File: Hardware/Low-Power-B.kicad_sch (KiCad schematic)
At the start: 25 parts, among them J1 01x02, Q1 BC557, Q2 BC547, Q3 BC557, Q4 BC547, Q5 BC547, U1 Arduino_Pro_Micro, U2 VS1838B

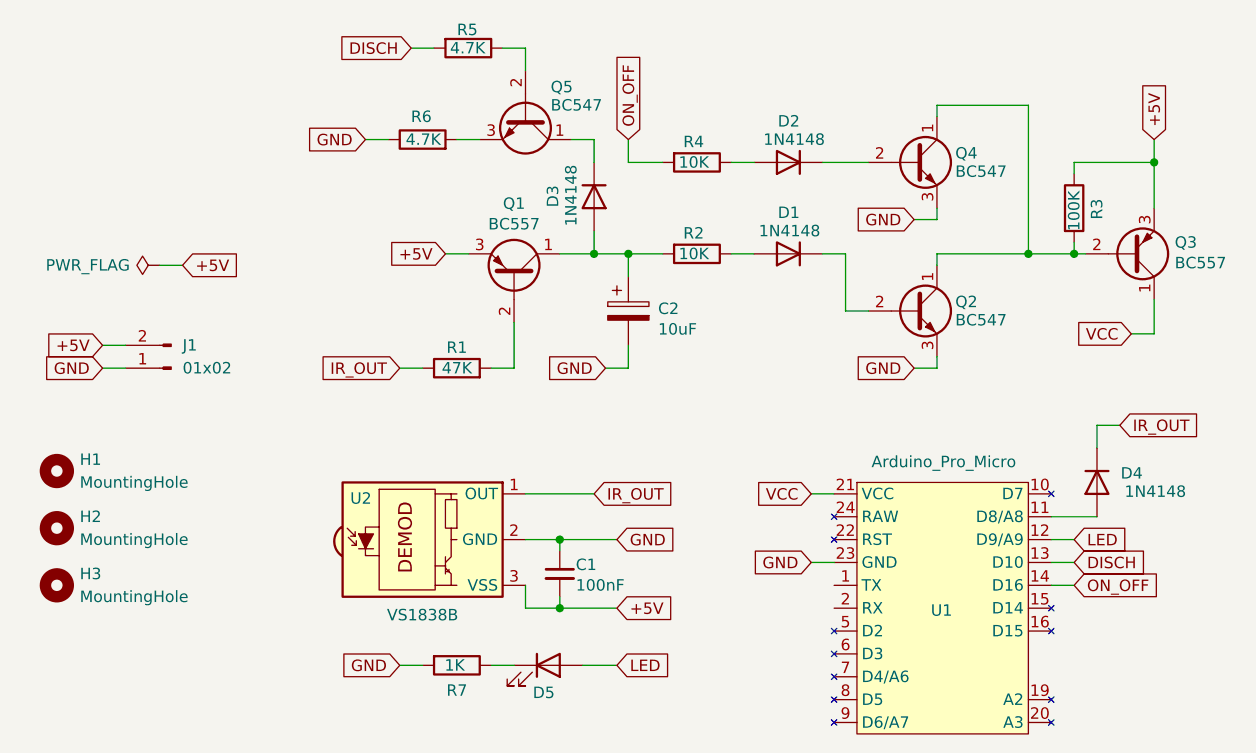
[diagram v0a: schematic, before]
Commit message: Minor fixes on Low-Power-B 3D model
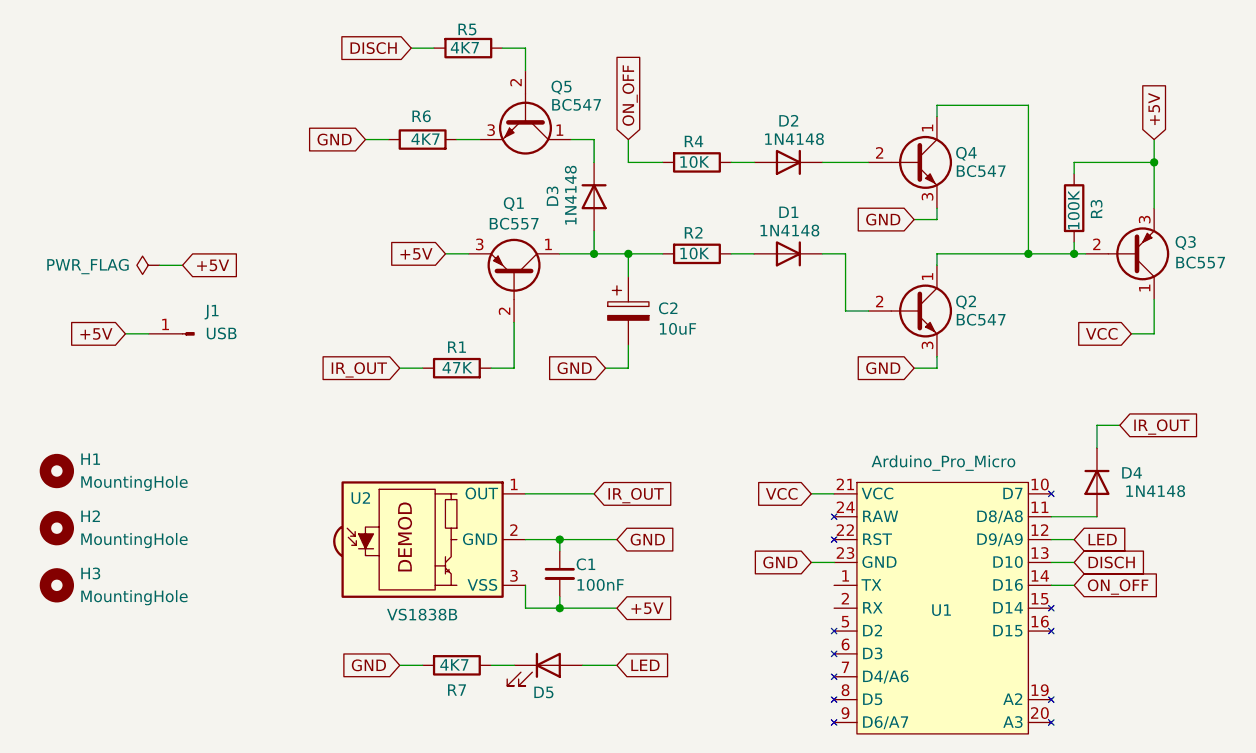
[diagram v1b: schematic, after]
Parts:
- J1: value 01x02 -> USB; footprint Connector_JST:JST_EH_B2B-EH-A_1x02_P2.50mm_Vertical -> Connector_Pin:Pin_D1.2mm_L11.3mm_W3.0mm_Flat; symbol Connector:Conn_01x02_Pin -> Connector:Conn_01x01_Pin
- R5, R6: value 4.7K -> 4K7
- R7: value 1K -> 4K7
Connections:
- net +5V: now also J1.1 (Pin_1); no longer J1.2 (Pin_2)
- net GND: no longer J1.1 (Pin_1)
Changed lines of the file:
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@@
 	(wire
 		(pts
-			(xy 90.17 86.36) (xy 92.71 86.36)
+			(xy 92.71 85.09) (xy 95.25 85.09)
 		)
 		(stroke
@@
 	(wire
 		(pts
-			(xy 90.17 88.9) (xy 92.71 88.9)
-		)
-		(stroke
-			(width 0)
-			(type default)
-		)
-	)
-	(wire
-		(pts
 			(xy 137.16 115.57) (xy 140.97 115.57)
 		)
@@
 		)
 	)
+	(global_label "IR_OUT"
+		(shape input)
+		(at 123.19 88.9 180)
+		(fields_autoplaced yes)
+		(effects
+			(font
+				(size 1.27 1.27)
+			)
+			(justify right)
+		)
+		(property "Intersheetrefs" "${INTERSHEET_REFS}"
+			(at 113.7338 88.9 0)
+			(effects
+				(font
+					(size 1.27 1.27)
+				)
+				(justify right)
+				(hide yes)
+			)
+		)
+	)
+	(global_label "DISCH"
+		(shape input)
+		(at 198.12 110.49 0)
+		(fields_autoplaced yes)
+		(effects
+			(font
+				(size 1.27 1.27)
+			)
+			(justify left)
+		)
+		(property "Intersheetrefs" "${INTERSHEET_REFS}"
+			(at 206.79 110.49 0)
+			(effects
+				(font
+					(size 1.27 1.27)
+				)
+				(justify left)
+				(hide yes)
+			)
+		)
+	)
+	(global_label "+5V"
+		(shape input)
+		(at 92.71 85.09 180)
+		(fields_autoplaced yes)
+		(effects
+			(font
+				(size 1.27 1.27)
+			)
+			(justify right)
+		)
+		(property "Intersheetrefs" "${INTERSHEET_REFS}"
+			(at 85.8543 85.09 0)
+			(effects
+				(font
+					(size 1.27 1.27)
+				)
+				(justify right)
+				(hide yes)
+			)
+		)
+	)
+	(global_label "LED"
+		(shape input)
+		(at 147.32 121.92 0)
+		(fields_autoplaced yes)
+		(effects
+			(font
+				(size 1.27 1.27)
+			)
+			(justify left)
+		)
+		(property "Intersheetrefs" "${INTERSHEET_REFS}"
+			(at 153.7523 121.92 0)
+			(effects
+				(font
+					(size 1.27 1.27)
+				)
+				(justify left)
+				(hide yes)
+			)
+		)
+	)
 	(global_label "GND"
 		(shape input)
-		(at 90.17 88.9 180)
+		(at 168.91 110.49 180)
 		(fields_autoplaced yes)
 		(effects
@@
 		)
 		(property "Intersheetrefs" "${INTERSHEET_REFS}"
-			(at 83.3143 88.9 0)
+			(at 162.0543 110.49 0)
 			(effects
 				(font
@@
 		)
 	)
-	(global_label "IR_OUT"
-		(shape input)
-		(at 123.19 88.9 180)
+	(global_label "GND"
+		(shape input)
+		(at 123.19 121.92 180)
 		(fields_autoplaced yes)
 		(effects
@@
 		)
 		(property "Intersheetrefs" "${INTERSHEET_REFS}"
-			(at 113.7338 88.9 0)
+			(at 116.3343 121.92 0)
 			(effects
 				(font
@@
 		)
 	)
-	(global_label "DISCH"
-		(shape input)
-		(at 198.12 110.49 0)
-		(fields_autoplaced yes)
-		(effects
-			(font
-				(size 1.27 1.27)
-			)
-			(justify left)
-		)
-		(property "Intersheetrefs" "${INTERSHEET_REFS}"
-			(at 206.79 110.49 0)
-			(effects
-				(font
-					(size 1.27 1.27)
-				)
-				(justify left)
-				(hide yes)
-			)
-		)
-	)
-	(global_label "+5V"
-		(shape input)
-		(at 90.17 86.36 180)
+	(global_label "VCC"
+		(shape input)
+		(at 204.47 85.09 180)
 		(fields_autoplaced yes)
 		(effects
@@
 		)
 		(property "Intersheetrefs" "${INTERSHEET_REFS}"
-			(at 83.3143 86.36 0)
+			(at 197.8562 85.09 0)
 			(effects
 				(font
@@
 		)
 	)
-	(global_label "LED"
-		(shape input)
-		(at 147.32 121.92 0)
-		(fields_autoplaced yes)
-		(effects
-			(font
-				(size 1.27 1.27)
-			)
-			(justify left)
-		)
-		(property "Intersheetrefs" "${INTERSHEET_REFS}"
-			(at 153.7523 121.92 0)
-			(effects
-				(font
-					(size 1.27 1.27)
-				)
-				(justify left)
-				(hide yes)
-			)
-		)
-	)
 	(global_label "GND"
 		(shape input)
-		(at 168.91 110.49 180)
+		(at 180.34 88.9 180)
 		(fields_autoplaced yes)
 		(effects
@@
 		)
 		(property "Intersheetrefs" "${INTERSHEET_REFS}"
-			(at 162.0543 110.49 0)
+			(at 173.4843 88.9 0)
 			(effects
 				(font
@@
 		)
 	)
-	(global_label "GND"
-		(shape input)
-		(at 123.19 121.92 180)
-		(fields_autoplaced yes)
-		(effects
-			(font
-				(size 1.27 1.27)
-			)
-			(justify right)
-		)
-		(property "Intersheetrefs" "${INTERSHEET_REFS}"
-			(at 116.3343 121.92 0)
-			(effects
-				(font
-					(size 1.27 1.27)
-				)
-				(justify right)
-				(hide yes)
-			)
-		)
-	)
-	(global_label "VCC"
-		(shape input)
-		(at 204.47 85.09 180)
-		(fields_autoplaced yes)
-		(effects
-			(font
-				(size 1.27 1.27)
-			)
-			(justify right)
-		)
-		(property "Intersheetrefs" "${INTERSHEET_REFS}"
-			(at 197.8562 85.09 0)
-			(effects
-				(font
-					(size 1.27 1.27)
-				)
-				(justify right)
-				(hide yes)
-			)
-		)
-	)
-	(global_label "GND"
-		(shape input)
-		(at 180.34 88.9 180)
-		(fields_autoplaced yes)
-		(effects
-			(font
-				(size 1.27 1.27)
-			)
-			(justify right)
-		)
-		(property "Intersheetrefs" "${INTERSHEET_REFS}"
-			(at 173.4843 88.9 0)
-			(effects
-				(font
-					(size 1.27 1.27)
-				)
-				(justify right)
-				(hide yes)
-			)
-		)
-	)
 	(symbol
-		(lib_id "Connector:Conn_01x02_Pin")
-		(at 97.79 88.9 180)
+		(lib_id "Connector:Conn_01x01_Pin")
+		(at 100.33 85.09 180)
 		(unit 1)
 		(exclude_from_sim no)
@@
 		(dnp no)
 		(property "Reference" "J1"
-			(at 99.06 86.3599 0)
+			(at 101.6 82.5499 0)
 			(effects
 				(font
@@
 			)
 		)
-		(property "Value" "01x02"
-			(at 99.06 88.8999 0)
+		(property "Value" "USB"
+			(at 101.6 85.0899 0)
 			(effects
 				(font
@@
 			)
 		)
-		(property "Footprint" "Connector_JST:JST_EH_B2B-EH-A_1x02_P2.50mm_Vertical"
-			(at 97.79 88.9 0)
+		(property "Footprint" "Connector_Pin:Pin_D1.2mm_L11.3mm_W3.0mm_Flat"
+			(at 100.33 85.09 0)
 			(effects
 				(font
@@
 		)
 		(property "Datasheet" "~"
-			(at 97.79 88.9 0)
-			(effects
-				(font
-					(size 1.27 1.27)
-				)
-				(hide yes)
-			)
-		)
-		(property "Description" "Generic connector, single row, 01x02, script generated"
-			(at 97.79 88.9 0)
-			(effects
-				(font
-					(size 1.27 1.27)
-				)
-				(hide yes)
-			)
-		)
-		(pin "2"
+			(at 100.33 85.09 0)
+			(effects
+				(font
+					(size 1.27 1.27)
+				)
+				(hide yes)
+			)
+		)
+		(property "Description" "Generic connector, single row, 01x01, script generated"
+			(at 100.33 85.09 0)
+			(effects
+				(font
+					(size 1.27 1.27)
+				)
+				(hide yes)
+			)
 		)
 		(pin "1"
@@
 			)
 		)
-		(property "Value" "4.7K"
+		(property "Value" "4K7"
 			(at 127.762 63.5 90)
 			(effects
@@
 			)
 		)
-		(property "Value" "1K"
+		(property "Value" "4K7"
 			(at 129.286 121.92 90)
 			(effects
@@
 			)
 		)
-		(property "Value" "4.7K"
+		(property "Value" "4K7"
 			(at 128.778 53.34 90)
 			(effects

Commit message: update README.md
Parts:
- removed H3: MountingHole, MountingHole:MountingHole_2.2mm_M2_ISO7380, symbol Mechanical:MountingHole
- J1: value USB -> USB_VBUS; footprint Connector_Pin:Pin_D1.2mm_L11.3mm_W3.0mm_Flat -> Connector_JST:JST_EH_B2B-EH-A_1x02_P2.50mm_Vertical; symbol Connector:Conn_01x01_Pin -> Connector:Conn_01x02_Pin
- R2: footprint Resistor_THT:R_Axial_DIN0204_L3.6mm_D1.6mm_P5.08mm_Horizontal -> Resistor_THT:R_Axial_DIN0207_L6.3mm_D2.5mm_P7.62mm_Horizontal
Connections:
- net VCC: now also J1.2 (Pin_2)
- net +5V renamed VBUS
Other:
- moved on the sheet: D4
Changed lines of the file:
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@@
+	(wire
+		(pts
+			(xy 200.66 104.14) (xy 200.66 105.41)
+		)
+		(stroke
+			(width 0)
+			(type default)
+		)
+	)
 	(wire
 		(pts
@@
 	(wire
 		(pts
+			(xy 200.66 105.41) (xy 195.58 105.41)
+		)
+		(stroke
+			(width 0)
+			(type default)
+		)
+	)
+	(wire
+		(pts
 			(xy 180.34 88.9) (xy 182.88 88.9)
 		)
@@
 	(wire
 		(pts
-			(xy 92.71 85.09) (xy 95.25 85.09)
+			(xy 97.79 86.36) (xy 95.25 86.36)
 		)
 		(stroke
@@
 	(wire
 		(pts
-			(xy 96.52 77.47) (xy 99.06 77.47)
+			(xy 95.25 78.74) (xy 97.79 78.74)
 		)
 		(stroke
@@
 	(wire
 		(pts
-			(xy 200.66 95.25) (xy 200.66 97.79)
+			(xy 200.66 95.25) (xy 200.66 96.52)
+		)
+		(stroke
+			(width 0)
+			(type default)
+		)
+	)
+	(wire
+		(pts
+			(xy 97.79 88.9) (xy 95.25 88.9)
 		)
 		(stroke
@@
 		(pts
 			(xy 160.02 66.04) (xy 162.56 66.04)
-		)
-		(stroke
-			(width 0)
-			(type default)
-		)
-	)
-	(wire
-		(pts
-			(xy 195.58 105.41) (xy 200.66 105.41)
 		)
 		(stroke
@@
 		)
 	)
-	(global_label "+5V"
+	(global_label "VBUS"
 		(shape input)
 		(at 128.27 76.2 180)
@@
 		)
 		(property "Intersheetrefs" "${INTERSHEET_REFS}"
-			(at 121.4143 76.2 0)
+			(at 120.3862 76.2 0)
 			(effects
 				(font
@@
 		)
 	)
+	(global_label "VCC"
+		(shape input)
+		(at 97.79 88.9 0)
+		(fields_autoplaced yes)
+		(effects
+			(font
+				(size 1.27 1.27)
+			)
+			(justify left)
+		)
+		(property "Intersheetrefs" "${INTERSHEET_REFS}"
+			(at 104.4038 88.9 0)
+			(effects
+				(font
+					(size 1.27 1.27)
+				)
+				(justify left)
+				(hide yes)
+			)
+		)
+	)
 	(global_label "GND"
 		(shape input)
@@
 		)
 	)
-	(global_label "+5V"
+	(global_label "VBUS"
 		(shape input)
 		(at 147.32 115.57 0)
@@
 		)
 		(property "Intersheetrefs" "${INTERSHEET_REFS}"
-			(at 154.1757 115.57 0)
+			(at 155.2038 115.57 0)
 			(effects
 				(font
@@
 		)
 	)
-	(global_label "+5V"
+	(global_label "VBUS"
 		(shape input)
 		(at 207.01 63.5 90)
@@
 		)
 		(property "Intersheetrefs" "${INTERSHEET_REFS}"
-			(at 207.01 56.6443 90)
+			(at 207.01 55.6162 90)
 			(effects
 				(font
@@
 		)
 	)
-	(global_label "+5V"
+	(global_label "VBUS"
 		(shape input)
-		(at 99.06 77.47 0)
+		(at 97.79 78.74 0)
 		(fields_autoplaced yes)
 		(effects
@@
 		)
 		(property "Intersheetrefs" "${INTERSHEET_REFS}"
-			(at 105.9157 77.47 0)
+			(at 105.6738 78.74 0)
 			(effects
 				(font
@@
 		)
 	)
-	(global_label "+5V"
+	(global_label "VBUS"
 		(shape input)
-		(at 92.71 85.09 180)
+		(at 97.79 86.36 0)
 		(fields_autoplaced yes)
 		(effects
@@
 				(size 1.27 1.27)
 			)
-			(justify right)
+			(justify left)
 		)
 		(property "Intersheetrefs" "${INTERSHEET_REFS}"
-			(at 85.8543 85.09 0)
-			(effects
-				(font
-					(size 1.27 1.27)
-				)
-				(justify right)
+			(at 105.6738 86.36 0)
+			(effects
+				(font
+					(size 1.27 1.27)
+				)
+				(justify left)
 				(hide yes)
 			)
@@
 	)
 	(symbol
-		(lib_id "Connector:Conn_01x01_Pin")
-		(at 100.33 85.09 180)
+		(lib_id "Connector:Conn_01x02_Pin")
+		(at 90.17 86.36 0)
 		(unit 1)
 		(exclude_from_sim no)
@@
 		(dnp no)
 		(property "Reference" "J1"
-			(at 101.6 82.5499 0)
+			(at 88.9 87.376 0)
 			(effects
 				(font
@@
 			)
 		)
-		(property "Value" "USB"
-			(at 101.6 85.0899 0)
+		(property "Value" "USB_VBUS"
+			(at 97.79 91.44 0)
 			(effects
 				(font
@@
 			)
 		)
-		(property "Footprint" "Connector_Pin:Pin_D1.2mm_L11.3mm_W3.0mm_Flat"
-			(at 100.33 85.09 0)
+		(property "Footprint" "Connector_JST:JST_EH_B2B-EH-A_1x02_P2.50mm_Vertical"
+			(at 90.17 86.36 0)
 			(effects
 				(font
@@
 		)
 		(property "Datasheet" "~"
-			(at 100.33 85.09 0)
-			(effects
-				(font
-					(size 1.27 1.27)
-				)
-				(hide yes)
-			)
-		)
-		(property "Description" "Generic connector, single row, 01x01, script generated"
-			(at 100.33 85.09 0)
+			(at 90.17 86.36 0)
+			(effects
+				(font
+					(size 1.27 1.27)
+				)
+				(hide yes)
+			)
+		)
+		(property "Description" "Generic connector, single row, 01x02, script generated"
+			(at 90.17 86.36 0)
 			(effects
 				(font
@@
 		)
 		(pin "1"
+		)
+		(pin "2"
 		)
 		(instances
@@
 		(lib_name "D_1")
 		(lib_id "Device:D")
-		(at 200.66 101.6 90)
+		(at 200.66 100.33 90)
 		(mirror x)
 		(unit 1)
@@
 		(dnp no)
 		(property "Reference" "D4"
-			(at 205.74 100.584 90)
+			(at 205.74 99.314 90)
 			(effects
 				(font
@@
 		)
 		(property "Value" "1N4148"
-			(at 210.566 102.616 90)
+			(at 210.566 101.346 90)
 			(effects
 				(font
@@
 		)
 		(property "Footprint" "Diode_THT:D_DO-35_SOD27_P7.62mm_Horizontal"
-			(at 213.106 101.6 0)
+			(at 213.106 100.33 0)
 			(effects
 				(font
@@
 		)
 		(property "Datasheet" "~"
-			(at 200.66 101.6 0)
+			(at 200.66 100.33 0)
 			(effects
 				(font
@@
 		)
 		(property "Description" "Diode"
-			(at 210.82 83.058 0)
+			(at 210.82 81.788 0)
 			(effects
 				(font
@@
 		)
 		(property "Sim.Device" "D"
-			(at 210.82 78.994 0)
+			(at 210.82 77.724 0)
 			(effects
 				(font
@@
 		)
 		(property "Sim.Pins" "1=K 2=A"
-			(at 211.074 91.694 0)
+			(at 211.074 90.424 0)
 			(effects
 				(font
@@
 		(pin "7"
 		)
-		(pin "16"
-		)
 		(pin "21"
 		)
@@
 		(pin "13"
 		)
-		(pin "20"
+		(pin "18"
 		)
 		(pin "19"
@@
 	)
 	(symbol
-		(lib_id "Mechanical:MountingHole")
-		(at 85.09 113.03 0)
-		(unit 1)
-		(exclude_from_sim no)
-		(in_bom no)
-		(on_board yes)
-		(dnp no)
-		(fields_autoplaced yes)
-		(property "Reference" "H3"
-			(at 87.63 111.7599 0)
-			(effects
-				(font
-					(size 1.27 1.27)
-				)
-				(justify left)
-			)
-		)
-		(property "Value" "MountingHole"
-			(at 87.63 114.2999 0)
-			(effects
-				(font
-					(size 1.27 1.27)
-				)
-				(justify left)
-			)
-		)
-		(property "Footprint" "MountingHole:MountingHole_2.2mm_M2_ISO7380"
-			(at 85.09 113.03 0)
-			(effects
-				(font
-					(size 1.27 1.27)
-				)
-				(hide yes)
-			)
-		)
-		(property "Datasheet" "~"
-			(at 85.09 113.03 0)
-			(effects
-				(font
-					(size 1.27 1.27)
-				)
-				(hide yes)
-			)
-		)
-		(property "Description" "Mounting Hole without connection"
-			(at 85.09 113.03 0)
-			(effects
-				(font
-					(size 1.27 1.27)
-				)
-				(hide yes)
-			)
-		)
-		(instances
-			(project "Low-Power-B"
-				(path "/58c9e19a-4594-4c28-bb07-5c5bf28794f4"
-					(reference "H3")
-					(unit 1)
-				)
-			)
-		)
-	)
-	(symbol
 		(lib_id "Device:R")
 		(at 156.21 76.2 270)
@@
 			)
 		)
-		(property "Footprint" "Resistor_THT:R_Axial_DIN0204_L3.6mm_D1.6mm_P5.08mm_Horizontal"
+		(property "Footprint" "Resistor_THT:R_Axial_DIN0207_L6.3mm_D2.5mm_P7.62mm_Horizontal"
 			(at 156.21 74.422 90)
 			(effects
@@
 	(symbol
 		(lib_id "power:PWR_FLAG")
-		(at 96.52 77.47 90)
+		(at 95.25 78.74 90)
 		(unit 1)
 		(exclude_from_sim no)
@@
 		(dnp no)
 		(property "Reference" "#FLG01"
-			(at 94.615 77.47 0)
+			(at 93.345 78.74 0)
 			(effects
 				(font
@@
 		)
 		(property "Value" "PWR_FLAG"
-			(at 93.218 77.47 90)
+			(at 91.948 78.74 90)
 			(effects
 				(font
@@
 		)
 		(property "Footprint" ""
-			(at 96.52 77.47 0)
+			(at 95.25 78.74 0)
 			(effects
 				(font
@@
 		)
 		(property "Datasheet" "~"
-			(at 96.52 77.47 0)
+			(at 95.25 78.74 0)
 			(effects
 				(font
@@
 		)
 		(property "Description" "Special symbol for telling ERC where power comes from"
-			(at 96.52 77.47 0)
-			(effects
-				(font
+			(at 95.25 78.74 0)
+			(effects
+				(font
